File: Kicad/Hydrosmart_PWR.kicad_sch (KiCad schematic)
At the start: 4 parts, among them U1 MAXM38643AEMB+

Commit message: + Created library and added information related to BOM: MANUFACTURER and MANUFACTURER PN
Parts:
- C1: symbol Hydrosmart_PWR-altium-import:root_0_b4654b650e69147ec39a6b967a45e02_Altium Content Vault -> HydSmart_VA:root_0_b4654b650e69147ec39a6b967a45e02_Altium Content Vault; MANUFACTURER (none) -> Taiyo Yuden; MANUFACTURER_NAME Taiyo Yuden -> (none); MANUFACTURER_PART_NUMBER JMK212BBJ476MG-T -> (none); MANUFACTURER PN (none) -> JMK212BBJ476MG-T
- C2: symbol Hydrosmart_PWR-altium-import:root_0_b4654b650e69147ec39a6b967a45e02_Altium Content Vault -> HydSmart_VA:root_0_b4654b650e69147ec39a6b967a45e02_Altium Content Vault; MANUFACTURER (none) -> Murata Electronics; MANUFACTURER_NAME Murata Electronics -> (none); MANUFACTURER_PART_NUMBER GRM158R60J226ME01D -> (none); MANUFACTURER PN (none) -> GRM158R60J226ME01D
- R1: symbol Hydrosmart_PWR-altium-import:root_1_RES_Altium Content Vault_0 -> HydSmart_VA:root_1_RES_Altium Content Vault_0; MANUFACTURER (none) -> Panasonic Electronic Components; MANUFACTURER_NAME Panasonic Electronic Components -> (none); MANUFACTURER_PART_NUMBER ERJ-2RKF2002X -> (none); MANUFACTURER PN (none) -> ERJ-2RKF2002X
- U1: symbol Hydrosmart_PWR-altium-import:root_0_MAXM38643AEMB+_* -> HydSmart_VA:root_0_MAXM38643AEMB+_*; MANUFACTURER (none) -> Analog Devices; MANUFACTURER_NAME Analog Devices -> (none); MANUFACTURER_PART_NUMBER MAXM38643AEMB+ -> (none); MANUFACTURER PN (none) -> MAXM38643AEMB+
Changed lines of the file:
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@@
 	)
 	(symbol
-		(lib_id "Hydrosmart_PWR-altium-import:root_0_MAXM38643AEMB+_*")
+		(lib_id "HydSmart_VA:root_0_MAXM38643AEMB+_*")
 		(at 124.46 88.9 0)
 		(unit 1)
@@
 			)
 		)
-		(property "MANUFACTURER_NAME" "Analog Devices"
-			(at 123.952 86.36 0)
-			(effects
-				(font
-					(size 1.27 1.27)
-				)
-				(justify left bottom)
-				(hide yes)
-			)
-		)
-		(property "MANUFACTURER_PART_NUMBER" "MAXM38643AEMB+"
-			(at 123.952 86.36 0)
-			(effects
-				(font
-					(size 1.27 1.27)
-				)
-				(justify left bottom)
-				(hide yes)
-			)
-		)
 		(property "MOUSER PART NUMBER" "700-MAXM38643AEMB+"
 			(at 123.952 86.36 0)
@@
 				)
 				(justify left bottom)
+				(hide yes)
+			)
+		)
+		(property "MANUFACTURER" "Analog Devices"
+			(at 124.46 88.9 0)
+			(effects
+				(font
+					(size 1.27 1.27)
+				)
+				(hide yes)
+			)
+		)
+		(property "MANUFACTURER PN" "MAXM38643AEMB+"
+			(at 124.46 88.9 0)
+			(effects
+				(font
+					(size 1.27 1.27)
+				)
 				(hide yes)
 			)
@@
 	)
 	(symbol
-		(lib_id "Hydrosmart_PWR-altium-import:root_1_RES_Altium Content Vault_0")
+		(lib_id "HydSmart_VA:root_1_RES_Altium Content Vault_0")
 		(at 108.966 107.95 0)
 		(unit 1)
@@
 			)
 		)
-		(property "MANUFACTURER_NAME" "Panasonic Electronic Components"
-			(at 110.744 99.822 0)
-			(effects
-				(font
-					(size 1.27 1.27)
-				)
-				(justify left bottom)
-				(hide yes)
-			)
-		)
-		(property "MANUFACTURER_PART_NUMBER" "ERJ-2RKF2002X"
-			(at 110.744 99.822 0)
-			(effects
-				(font
-					(size 1.27 1.27)
-				)
-				(justify left bottom)
+		(property "MANUFACTURER" "Panasonic Electronic Components"
+			(at 108.966 107.95 0)
+			(effects
+				(font
+					(size 1.27 1.27)
+				)
+				(hide yes)
+			)
+		)
+		(property "MANUFACTURER PN" "ERJ-2RKF2002X"
+			(at 108.966 107.95 0)
+			(effects
+				(font
+					(size 1.27 1.27)
+				)
 				(hide yes)
 			)
@@
 	)
 	(symbol
-		(lib_id "Hydrosmart_PWR-altium-import:root_0_b4654b650e69147ec39a6b967a45e02_Altium Content Vault")
+		(lib_id "HydSmart_VA:root_0_b4654b650e69147ec39a6b967a45e02_Altium Content Vault")
 		(at 162.306 91.44 0)
 		(unit 1)
@@
 			)
 		)
-		(property "Description" "Chip Multilayer Ceramic Capacitors for General Purpose, 0402, 22uF, X5R, 15%, 20%, 10V"
+		(property "Description" "Multilayer Ceramic Capacitors 47μF ±20% 6.3V X5R SMD 0805"
 			(at 162.306 91.44 0)
 			(effects
@@
 			)
 		)
-		(property "MANUFACTURER_NAME" "Murata Electronics"
-			(at 159.512 90.932 0)
-			(effects
-				(font
-					(size 1.27 1.27)
-				)
-				(justify left bottom)
-				(hide yes)
-			)
-		)
-		(property "MANUFACTURER_PART_NUMBER" "GRM158R60J226ME01D"
-			(at 159.512 90.932 0)
-			(effects
-				(font
-					(size 1.27 1.27)
-				)
-				(justify left bottom)
+		(property "MANUFACTURER" "Murata Electronics"
+			(at 162.306 91.44 0)
+			(effects
+				(font
+					(size 1.27 1.27)
+				)
+				(hide yes)
+			)
+		)
+		(property "MANUFACTURER PN" "GRM158R60J226ME01D"
+			(at 162.306 91.44 0)
+			(effects
+				(font
+					(size 1.27 1.27)
+				)
 				(hide yes)
 			)
@@
 	)
 	(symbol
-		(lib_id "Hydrosmart_PWR-altium-import:root_0_b4654b650e69147ec39a6b967a45e02_Altium Content Vault")
+		(lib_id "HydSmart_VA:root_0_b4654b650e69147ec39a6b967a45e02_Altium Content Vault")
 		(at 101.346 91.694 0)
 		(unit 1)
@@
 			)
 		)
-		(property "MANUFACTURER_NAME" "Taiyo Yuden"
-			(at 98.552 91.186 0)
-			(effects
-				(font
-					(size 1.27 1.27)
-				)
-				(justify left bottom)
-				(hide yes)
-			)
-		)
-		(property "MANUFACTURER_PART_NUMBER" "JMK212BBJ476MG-T"
-			(at 98.552 91.186 0)
-			(effects
-				(font
-					(size 1.27 1.27)
-				)
-				(justify left bottom)
-				(hide yes)
-			)
+		(property "MANUFACTURER" "Taiyo Yuden"
+			(at 101.346 91.694 0)
+			(effects
+				(font
+					(size 1.27 1.27)
+				)
+				(hide yes)
+			)
+		)
+		(property "MANUFACTURER PN" "JMK212BBJ476MG-T"
+			(at 101.346 91.694 0)
+			(effects
+				(font
+					(size 1.27 1.27)
+				)
+				(hide yes)
+			)

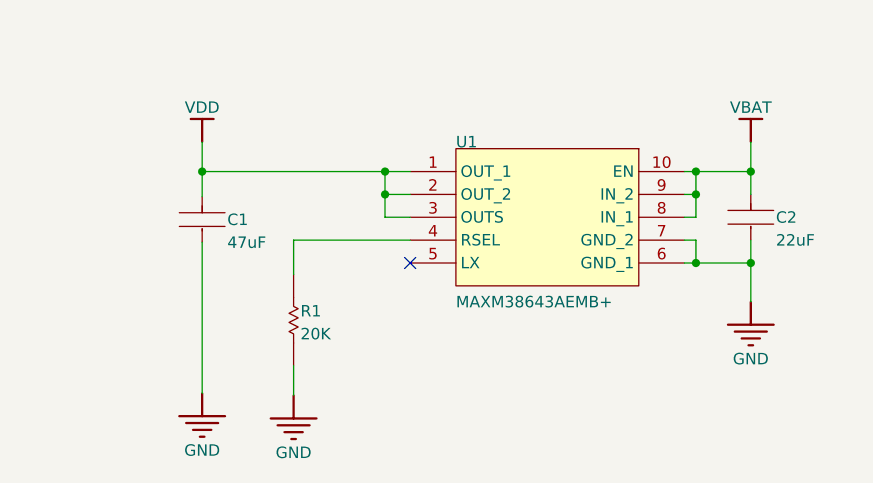
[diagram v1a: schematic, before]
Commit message: VB changes start. Updated regulator and added test points
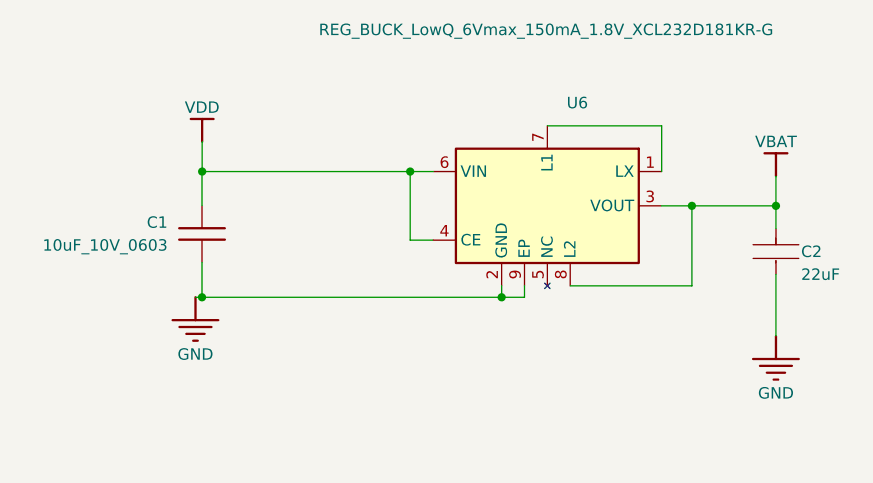
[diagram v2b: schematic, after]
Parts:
- removed C1: ${CAPACITANCE}, HydSmart_VA:FP-C2012-125-0_2-MFG, symbol HydSmart_VA:root_0_b4654b650e69147ec39a6b967a45e02_Altium Content Vault
- removed R1: ${ALTIUM_VALUE}, HydSmart_VA:R0402, symbol HydSmart_VA:root_1_RES_Altium Content Vault_0
- removed U1: MAXM38643AEMB+, HydSmart_VA:MAXM38643AEMB, symbol HydSmart_VA:root_0_MAXM38643AEMB+_*
- added C1: 10uF_10V_0603, Capacitor_SMD:C_0603_1608Metric, symbol aa_standard:CAP CER 10UF 10V X5R 0603
- added U6: REG_BUCK_LowQ_6Vmax_150mA_1.8V_XCL232D181KR-G, aa_footprints:XCL232B051KRG, symbol aa_ic:REG_BUCK_LowQ_6Vmax_150mA_1.8V_XCL232D181KR-G
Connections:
- net GND: now also C1.1, U6.2 (GND), U6.9 (EP)
- net VBAT: now also U6.3 (VOUT), U6.8 (L2)
- net VDD: now also C1.2, U6.4 (CE), U6.6 (VIN)
- new net: U6.1 (LX), U6.7 (L1)
- no-connect marks 1 -> 0
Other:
- moved on the sheet: C2
